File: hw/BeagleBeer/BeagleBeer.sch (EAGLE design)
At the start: 96 parts

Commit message: Route BeagleBeer Flying Squirrel Controller PCB.
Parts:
- removed C8: 0.1 uF, geoffculp:CAP0805
- removed U$42: CAT24C256WI-GT3, ON Semiconductor_By_element14_Batch_1:CAT24C256WI-GT3
- added R35, R36, R37, R38: 10K, geoffculp:RESISTOR0805-RES
- added U5: CAT24C256WI-GT3, ON Semiconductor_By_element14_Batch_1:CAT24C256WI-GT3
- U$2: value BEAGLEBONE_OUTLINE -> BEAGLEBONE_OUTLINEBEAGLEBEER; device microbuilder:BEAGLEBONE_OUTLINE -> adafruit:BEAGLEBONE_OUTLINEBEAGLEBEER
- renumbered U$7 to U1
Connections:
- removed net AVCC: C7.1, JP1.4, U$2.GPIO2_12
- removed net I2C1_SCA: U$42.SDA
- removed net I2C1_SCL: JP3.15, U$2.I2C1_SCL
- removed net N$104: U4.A8
- removed net N$105: U4.A7
- removed net N$11: JP1.13, U$2.GPIO1_30
- removed net N$12: JP1.12, U$2.GPIO1_4
- removed net N$13: JP1.11, U$2.GPIO1_0
- removed net N$14: JP1.10, U$2.GPIO2_22
- removed net N$15: JP1.9, U$2.GPIO2_23
- removed net N$21: JP1.3, U$2.GPIO2_10
- removed net N$22: JP1.2, U$2.GPIO2_8
- removed net N$23: JP1.1, U$2.GPIO2_6
- removed net N$24: R19.1
- removed net N$29: JP2.6, U$2.GPIO1_12
- removed net N$30: JP2.7, U$2.GPIO0_26
- removed net N$31: JP2.8, U$2.GPIO1_14
- removed net N$32: JP2.9, U$2.GPIO2_1
- removed net N$43: JP2.20, U$2.GPIO2_13
- removed net N$44: JP2.21, U$2.GPIO2_11
- removed net N$47: JP1.22, U$2.GPIO1_6
- removed net N$48: JP1.21, U$2.GPIO1_2
- removed net N$56: JP3.14, U$2.I2C2_SCL
- removed net N$58: JP3.12, U$2.GPIO1_17
- removed net N$59: JP3.11, U$2.GPIO3_21
- removed net N$6: JP1.18, U$2.GPIO1_13
- removed net N$78: JP4.9, U$2.I2C1_SDA
- removed net N$79: JP4.10, U$2.I2C2_SDA
- removed net N$8: JP1.16, U$2.GPIO1_15
- removed net N$9: JP1.15, U$2.GPIO0_27
- new net ALARM_3P3: JP3.12, U$2.GPIO1_17, U4.A7
- new net EEPROM_SCA: U5.SDA
- new net EEPROM_SCL: JP3.15, R36.1, U$2.I2C1_SCL, U5.SCL
- new net EEPROM_SDA: JP4.9, R38.1, U$2.I2C1_SDA
- new net LCD_SCL: JP3.14, R35.1, U$2.I2C2_SCL
- new net LCD_SDA: JP4.10, R37.1, U$2.I2C2_SDA
- new net RESET_3P3: JP3.11, U$2.GPIO3_21, U4.A8
- net 3.3V: now also C2.1, C6.1, C7.1, R35.2, R36.2, R37.2, R38.2, U5.VCC; no longer C8.1
- net 5V: now also R19.1
- net BUZZER_3P3: now also JP1.10, U$2.GPIO2_22
- net FLOW_C: no longer U2.B3
- net FLOW_C_3P3: now also JP2.6, U$2.GPIO1_12; no longer U2.A3
- net FLOW_D: no longer U2.B4
- net FLOW_D_3P3: now also JP2.7, U$2.GPIO0_26; no longer U2.A4
- net GND: now also U5.A0, U5.A1, U5.A2, U5.VSS; no longer C8.2, U$42.A1, U$42.VSS
- net GPIO_A_3P3: now also JP1.15, U$2.GPIO0_27
- net GPIO_B_3P3: now also JP1.13, U$2.GPIO1_30
- net GPIO_C_3P3: now also JP1.12, U$2.GPIO1_4
- net GPIO_D_3P3: now also JP1.11, U$2.GPIO1_0
- net GPIO_E: no longer U4.B8
- net LED_FLOW_A: no longer U2.B5
- net LED_FLOW_A_3P3: now also JP2.8, U$2.GPIO1_14; no longer U2.A5
- net LED_FLOW_B: no longer U2.B6
- net LED_FLOW_B_3P3: now also JP2.9, U$2.GPIO2_1; no longer U2.A6
- net LED_FLOW_C_3P3: now also JP2.20, U$2.GPIO2_13
- net LED_FLOW_D_3P3: now also JP2.21, U$2.GPIO2_11
- net N$102: now also TP2.TP, U5.WP; no longer U$42.WP
- net ONEWIRE_A_3P3: now also JP1.22, U$2.GPIO1_6
- net ONEWIRE_B_3P3: now also JP1.21, U$2.GPIO1_2
- net ONEWIRE_C_3P3: now also JP1.18, U$2.GPIO1_13
- net ONEWIRE_D_3P3: now also JP1.16, U$2.GPIO1_15
- net RELAY_A_3P3: now also JP1.4, U$2.GPIO2_12
- net RELAY_B_3P3: now also JP1.3, U$2.GPIO2_10
- net RELAY_C_3P3: now also JP1.2, U$2.GPIO2_8
- net RELAY_D_3P3: now also JP1.1, U$2.GPIO2_6
- net RESET: now also U4.B8
- net TEST_PULSE_3P3: now also JP1.9, U$2.GPIO2_23
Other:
- moved on the sheet: C2, C6, C7, JP1, JP2, JP3, JP4, R19, R34, TP2, U$2

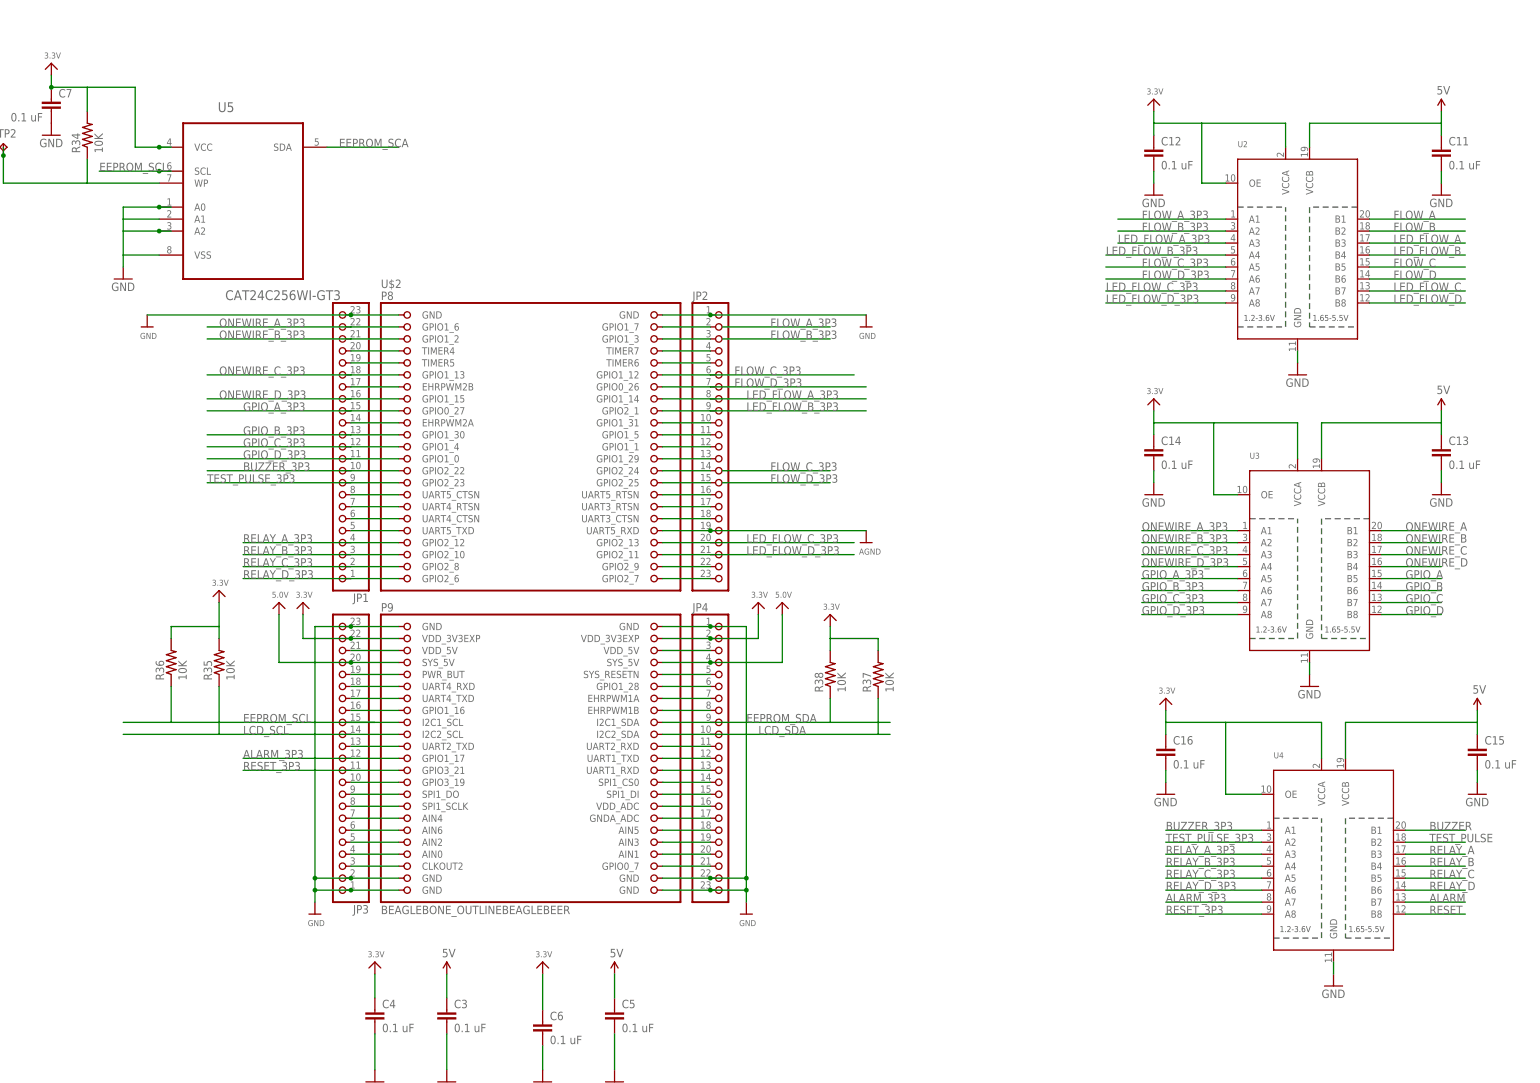
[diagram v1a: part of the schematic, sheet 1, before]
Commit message: Run ERC on Controller and reroute.
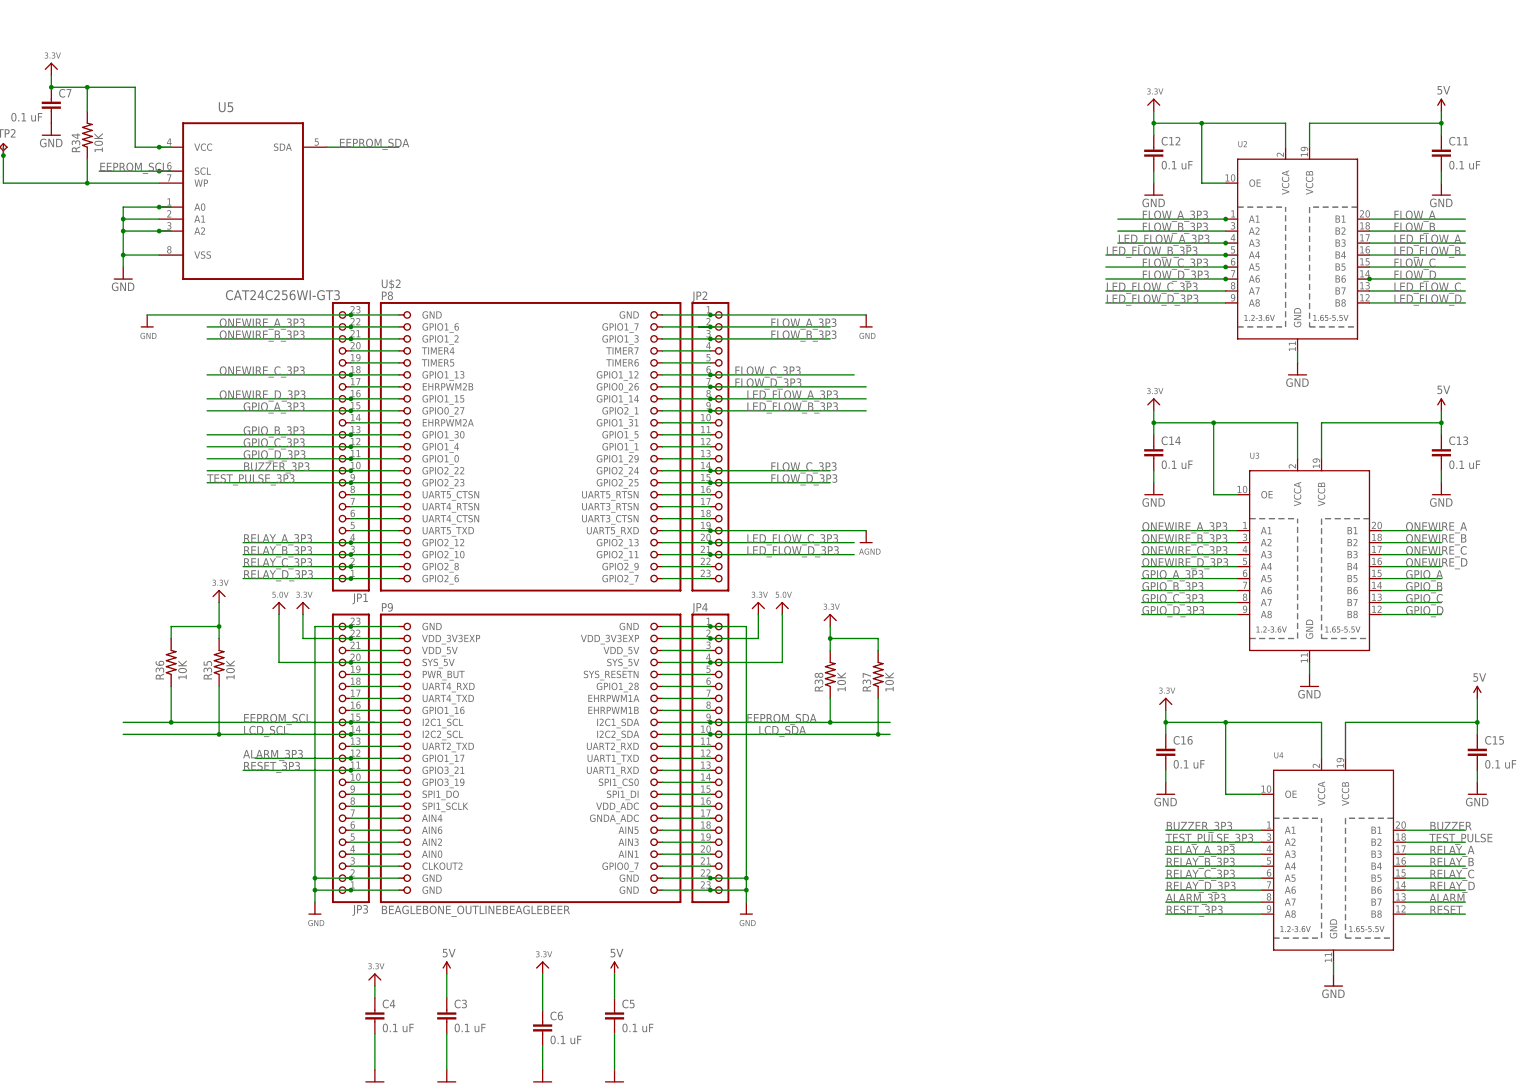
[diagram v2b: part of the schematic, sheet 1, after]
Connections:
- removed net EEPROM_SCA: U5.SDA
- removed net GPIO_E: HEADER-GPO.2
- removed net N$2: R26.2, R27.2
- removed net N$20: R17.2, R18.2
- removed net N$3: R15.2, R16.2
- removed net N$37: JP2.14, U$2.GPIO2_24
- removed net N$38: JP2.15, U$2.GPIO2_25
- removed net N$50: JP2.2, U$2.GPIO1_7
- removed net N$68: JP2.3, U$2.GPIO1_3
- new net FLOW_A_3P3: JP2.2, U$2.GPIO1_7, U2.A1
- net 3.3V: now also C4.1
- net 5V: now also R15.2, R16.2, R17.2, R18.2, R26.2, R27.2, U1.VCC
- net EEPROM_SDA: now also U5.SDA
- net FLOW_B_3P3: now also JP2.3, U$2.GPIO1_3
- net FLOW_C: now also U2.B5
- net FLOW_C_3P3: now also JP2.14, U$2.GPIO2_24, U2.A5
- net FLOW_D: now also U2.B6
- net FLOW_D_3P3: now also JP2.15, U$2.GPIO2_25, U2.A6
- net LED_FLOW_A: now also U2.B3
- net LED_FLOW_A_3P3: now also U2.A3
- net LED_FLOW_B: now also U2.B4
- net LED_FLOW_B_3P3: now also U2.A4
- net RESET: now also HEADER-GPO.2
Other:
- moved on the sheet: R30

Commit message: update archive with as built files
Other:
- note added: "BeagleBeer Controller"
- note removed: "v1.1"
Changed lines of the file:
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@@
 <part name="GND40" library="SparkFun" deviceset="GND" device=""/>
 <part name="GND41" library="SparkFun" deviceset="GND" device=""/>
-<part name="FRAME3" library="dframes" deviceset="US_11X17" device=""/>
-<part name="FRAME1" library="dframes" deviceset="US_11X17" device=""/>
 <part name="R34" library="geoffculp" deviceset="RESISTOR" device="0805-RES" value="10K"/>
 <part name="TP2" library="testpad" deviceset="TP" device="TP18SQ"/>
@@
 <part name="R35" library="geoffculp" deviceset="RESISTOR" device="0805-RES" value="10K"/>
 <part name="R30" library="geoffculp" deviceset="RESISTOR" device="0805-RES" value="10K"/>
+<part name="FRAME1" library="dframes" deviceset="US_11X17" device="">
+<attribute name="CHECKED" value="Robin Coxe"/>
+<attribute name="COMPANY" value="Venture Cafe Foundation"/>
+<attribute name="DATE" value="8-FEB-2013"/>
+<attribute name="DRAWN" value="Robin Coxe"/>
+<attribute name="DRGNO" value="2"/>
+<attribute name="REV" value="0"/>
+</part>
+<part name="FRAME2" library="dframes" deviceset="US_11X17" device="">
+<attribute name="CHECKED" value="Robin Coxe"/>
+<attribute name="COMPANY" value="Venture Cafe Foundation"/>
+<attribute name="DATE" value="8-FEB-2013"/>
+<attribute name="DRAWN" value="Robin Coxe"/>
+<attribute name="DRGNO" value="2"/>
+<attribute name="REV" value="0"/>
+</part>
 </parts>
 <sheets>
 <sheet>
 <plain>
+<text x="342.9" y="17.78" size="3.81" layer="94">BeagleBeer Controller</text>
 </plain>
 <instances>
@@
 <instance part="GND40" gate="1" x="294.64" y="114.3"/>
 <instance part="GND41" gate="1" x="299.72" y="50.8"/>
-<instance part="FRAME3" gate="G$1" x="0" y="-2.54" smashed="yes"/>
-<instance part="FRAME3" gate="G$2" x="307.34" y="0"/>
-<instance part="FRAME3" gate="G$4" x="0" y="276.86"/>
 <instance part="R34" gate="G$1" x="35.56" y="231.14" rot="R90"/>
 <instance part="TP2" gate="G$1" x="17.78" y="229.362"/>
@@
 <instance part="U$2" gate="G$1" x="129.54" y="132.08"/>
 <instance part="R35" gate="G$1" x="63.5" y="119.38" rot="R90"/>
+<instance part="FRAME2" gate="G$1" x="0" y="0">
+<attribute name="CHECKED" x="0" y="0" size="1.778" layer="96"/>
+<attribute name="COMPANY" x="0" y="0" size="1.778" layer="96"/>
+<attribute name="DATE" x="0" y="0" size="1.778" layer="96"/>
+<attribute name="DRAWN" x="0" y="0" size="1.778" layer="96"/>
+<attribute name="DRGNO" x="0" y="0" size="1.778" layer="96" display="off"/>
+<attribute name="REV" x="0" y="0" size="1.778" layer="96" display="off"/>
+</instance>
+<instance part="FRAME2" gate="G$2" x="309.88" y="0"/>
+<instance part="FRAME2" gate="G$4" x="2.54" y="276.86"/>
 </instances>
 <busses>
@@
 <net name="LED_FLOW_A_3P3" class="0">
 <segment>
-<wire x1="160.02" y1="284.48" x2="160.02" y2="261.62" width="0.1524" layer="91"/>
-<label x="160.02" y="261.62" size="1.778" layer="95" rot="R90"/>
-</segment>
-<segment>
 <wire x1="276.86" y1="208.28" x2="254" y2="208.28" width="0.1524" layer="91"/>
 <label x="254" y="208.28" size="1.778" layer="95"/>
@@
 </net>
 <net name="LED_FLOW_B_3P3" class="0">
-<segment>
-<wire x1="162.56" y1="284.48" x2="162.56" y2="261.62" width="0.1524" layer="91"/>
-<label x="162.56" y="261.62" size="1.778" layer="95" rot="R90"/>
-</segment>
 <segment>
 <wire x1="276.86" y1="205.74" x2="251.46" y2="205.74" width="0.1524" layer="91"/>
@@
 <sheet>
 <plain>
-<text x="330.2" y="15.24" size="2.54" layer="94">v1.1</text>
+<text x="342.9" y="17.78" size="3.81" layer="94">BeagleBeer Controller</text>
 </plain>
 <instances>
@@
 <instance part="C2" gate="G$1" x="22.86" y="25.4"/>
 <instance part="U$30" gate="G$1" x="22.86" y="38.1"/>
-<instance part="FRAME1" gate="G$1" x="0" y="-2.54"/>
-<instance part="FRAME1" gate="G$2" x="309.88" y="-2.54"/>
-<instance part="FRAME1" gate="G$4" x="2.54" y="274.32"/>
 <instance part="R30" gate="G$1" x="106.68" y="127" rot="R90"/>
+<instance part="FRAME1" gate="G$1" x="0" y="0">
+<attribute name="CHECKED" x="0" y="0" size="1.778" layer="96"/>
+<attribute name="COMPANY" x="0" y="0" size="1.778" layer="96"/>
+<attribute name="DATE" x="0" y="0" size="1.778" layer="96"/>
+<attribute name="DRAWN" x="0" y="0" size="1.778" layer="96"/>
+<attribute name="DRGNO" x="0" y="0" size="1.778" layer="96"/>
+<attribute name="REV" x="0" y="0" size="1.778" layer="96"/>
+</instance>
+<instance part="FRAME1" gate="G$2" x="309.88" y="0"/>
+<instance part="FRAME1" gate="G$4" x="2.54" y="276.86"/>
 </instances>
 <busses>
